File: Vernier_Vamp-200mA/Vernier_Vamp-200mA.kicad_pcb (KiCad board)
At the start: 4 copper layers, 143 x 99.5 mm, 203 parts, among them J1 Conn_01x02, J2 RJ45, J3 Screw_Terminal_01x04, J4 Conn_02x07_Odd_Even, J5 Conn_Coaxial, J6 Conn_Coaxial, J7 Conn_Coaxial, Q1 Si4447ADY, Q2 IRF8707PbF, SW1 DPDT_Hirose, U1 LM4040DBZ-5, U10 OPA2277, U11 OPA2277, U12 OPA2277, U13 OPA2277, U14 OPA2277, U15 OPA1622, U16 OPA1622, U17 OPA1622, U2 LM4040DBZ-5, U3 LM393, U4 TPS7A470x, U5 TPS7A470x, U6 TPS7A33, U7 LTC6655-2.5, U8 DAC8814, U9 OPA2277

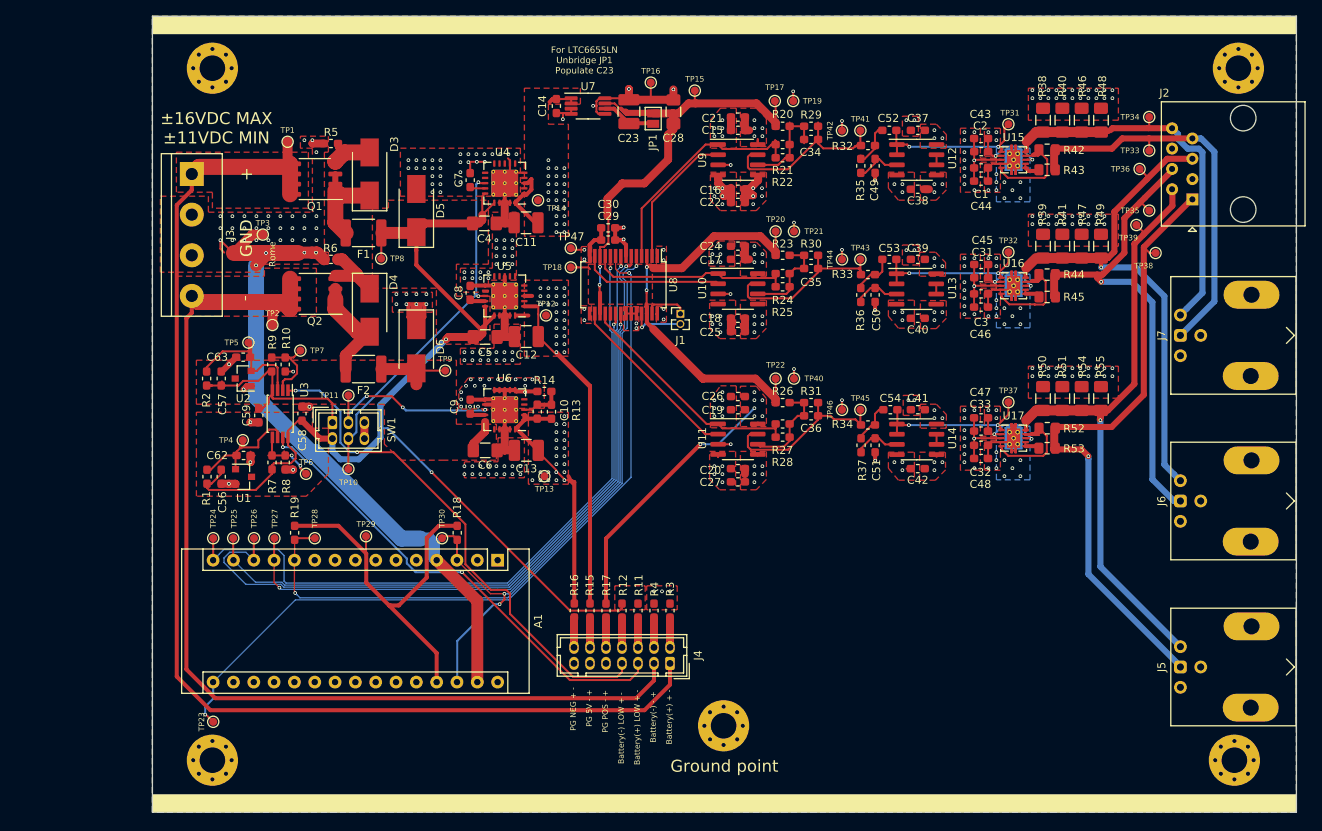
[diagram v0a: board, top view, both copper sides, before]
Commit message: Coil driver version 1.0B
Updated coil driver 200mA version with fixes requested by Iain.
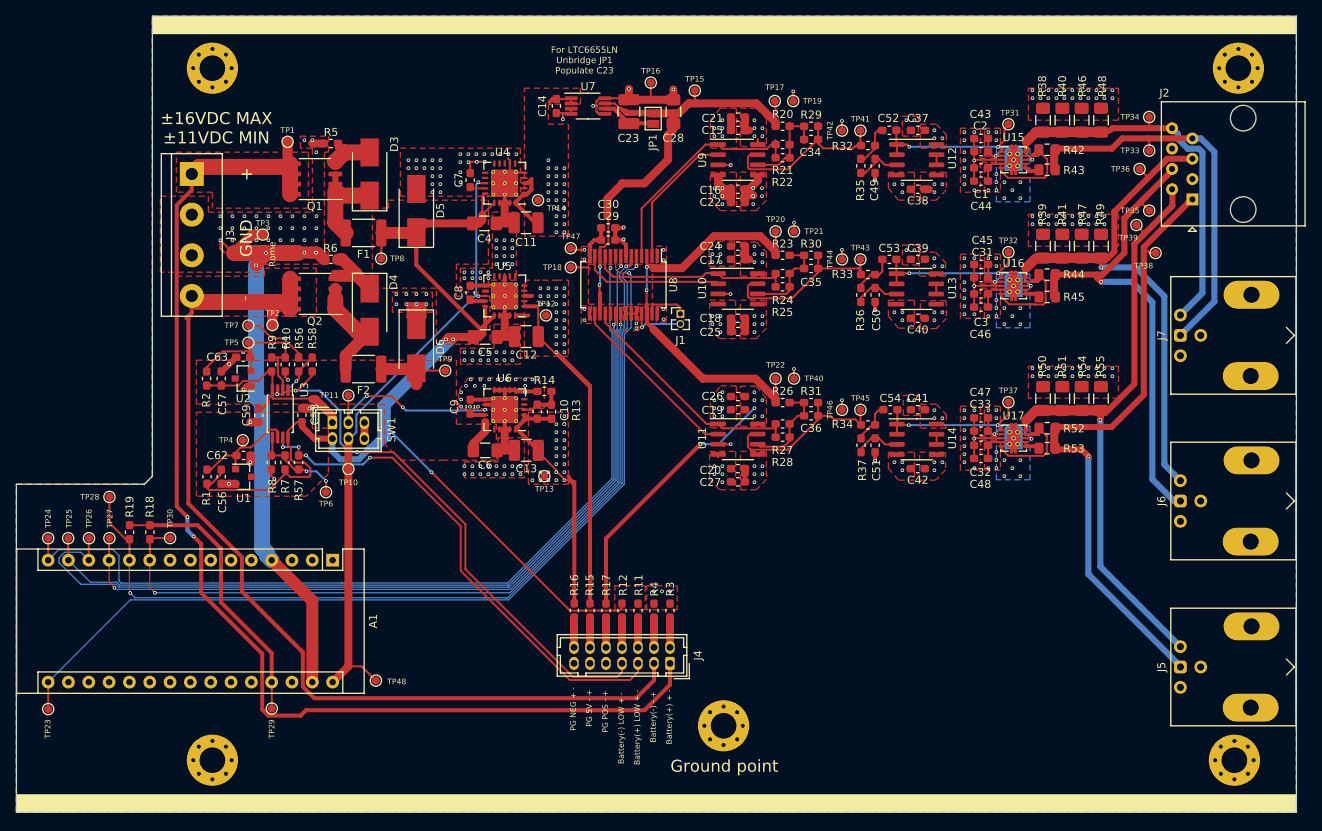
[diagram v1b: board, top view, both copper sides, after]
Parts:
- added R56: 3k, Resistor_SMD:R_0603_1608Metric_Pad1.05x0.95mm_HandSolder, F.Cu at (61.8, 91.3)
- added R57: 2M, Resistor_SMD:R_0603_1608Metric_Pad1.05x0.95mm_HandSolder, F.Cu at (61.8, 103.5)
- added R58: 133k, Resistor_SMD:R_0603_1608Metric_Pad1.05x0.95mm_HandSolder, F.Cu at (63.5, 91.3)
- added TP48: TestPoint_Probe, TestPoint:TestPoint_Pad_D1.0mm, F.Cu at (71.4, 130.8)
- R9: value 120k -> 133k
- moved R18 38.4 mm to (43.2, 112.2)
- moved TP30 34.0 mm to (45.7, 113.0)
- moved TP28 26.2 mm to (38.1, 107.8), turned to 0 degrees
- moved TP29 24.6 mm to (58.4, 134.3)
- moved TP23 20.7 mm to (30.5, 134.4)
- moved R19 20.6 mm to (40.6, 112.2)
- moved A1 20.6 mm to (66.0, 115.8)
- moved TP24 20.6 mm to (30.5, 113.0)
- moved TP25 20.6 mm to (33.0, 113.0)
- moved TP26 20.6 mm to (35.6, 113.0)
- moved TP27 20.6 mm to (38.1, 113.0)
- moved TP7 7.21 mm to (55.5, 86.4), turned to 180 degrees
- moved TP6 3.40 mm to (65.2, 107.2), turned to 180 degrees
- moved R8 1.74 mm to (58.4, 103.5)
- moved R7 1.62 mm to (60.1, 103.5)
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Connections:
- net +8V renamed +7V5
- net -8V renamed -7V5
- net /Power/+5V_c_ref renamed /Power/Battery_Management/+5V_c_ref
- net /Power/LED1_N renamed /Power/Battery_Management/Battery+_C
- net /Power/LED2_P renamed /Power/Battery_Management/Battery-_A
- net /Power/LED3_N renamed /Power/Battery_Management/Battery+_LOW_C
- net /Power/LED3_P renamed /Power/Battery_Management/Battery+_LOW_A
- net /Power/LED4_N renamed /Power/Battery_Management/Battery-_LOW_C
- net /Power/LED4_P renamed /Power/Battery_Management/Battery-_LOW_A
- net /Power/LED5_P renamed /Power/Battery_Management/+7.5_PG_A
- net /Power/LED6_P renamed /Power/Battery_Management/+5_PG_A
- net /Power/LED7_N renamed /Power/Battery_Management/-7.5_PG_C
- A1 pad 10: Net-(A1-Pad10) -> /DAC/~RS
- A1 pad 28: /DAC/~RS -> Net-(A1-Pad28)
- A1 pad 3: /DAC/~RS -> Net-(A1-Pad3)
- A1 pad 30: Net-(A1-Pad30) -> +12V_batt_post
- C63 pad 1: /Power/-5V_c_ref -> /Power/Battery_Management/-5V_c_ref
- R2 pad 1: /Power/-5V_c_ref -> /Power/Battery_Management/-5V_c_ref
- SW1 pad 4: /Power/+EN -> +12V_batt_post
- TP10 pad 1: /Power/+EN -> +12V_batt_post
- TP5 pad 1: /Power/-5V_c_ref -> /Power/Battery_Management/-5V_c_ref
- U2 pad 2: /Power/-5V_c_ref -> /Power/Battery_Management/-5V_c_ref
- U3 pad 3: /Power/-5V_c_ref -> Net-(R56-Pad1)
- U4 pad 13: /Power/+EN -> +12V_batt_post
- U5 pad 13: /Power/+EN -> +12V_batt_post
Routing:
- net +12V_batt_post: track 0.00 -> 76.6 mm, vias 0 -> 2
- net /Power/+EN: track 44.9 -> 0.00 mm, vias 2 -> 0
- net /DAC/~RS: track 76.1 -> 103.1 mm, vias 3 -> 2
- net /DAC/MSB: track 86.3 -> 111.2 mm
- net /Power/+12VDC_bat: track 143.0 -> 167.3 mm, vias 3 -> 4
- net /DAC/SDO: track 78.0 -> 98.6 mm
- net /DAC/SDI: track 90.2 -> 110.8 mm
- net /DAC/~LDAC: track 75.6 -> 96.3 mm
- net /DAC/~CS: track 91.9 -> 112.5 mm
- net /Power/Battery_Management/-5V_c_ref: track 0.00 -> 18.4 mm
- net /Power/-5V_c_ref: track 18.4 -> 0.00 mm
- net /DAC/CLK: track 97.8 -> 116.0 mm, vias 2 -> 1
- net +5VD: track 47.8 -> 35.4 mm
- net GNDD: track 67.8 -> 57.1 mm
- net -BATT: track 130.7 -> 123.6 mm
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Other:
- board size 143 x 99.5 mm -> 160 x 99.5 mm
- board text added: "Vernier Vamp 200mA Rev 1.0B Designer: Marcin Mrozowski EQOP"
- board text removed: "Vernier Vamp 200mA Rev 1.0A EQOP"

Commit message: Schematic and layout changes
Schematic updates:
- Added extra comments
- Added description (BNC channels)
- Moved mounting holes to the title block
- Added an option for connecting low battery indicatior LEDs to either +12V or GND (Comparator pulls to -12V)
- Added a 0R resistor for connecting +12V to Vin of nano
Layout:
- Added board ID and datecode on both sides
- Fixed priority of GND copper islands that were causing issues
- Changed the ground plane to be solid on the connection point (still not ideal but better)
- All components with thermal vias require tented vias so left as default
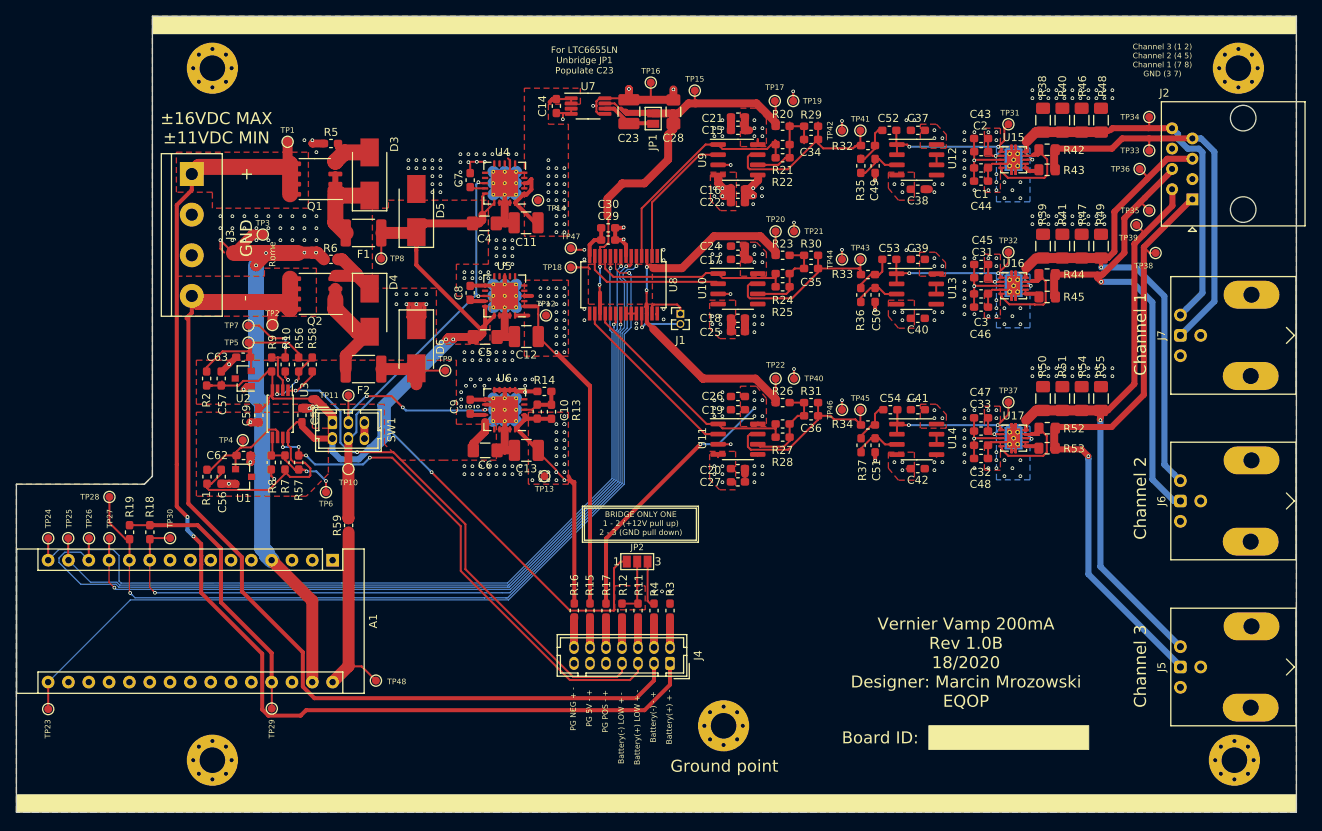
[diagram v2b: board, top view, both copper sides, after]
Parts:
- added JP2: SolderJumper_3_Open, Jumper:SolderJumper-3_P1.3mm_Open_Pad1.0x1.5mm_NumberLabels, F.Cu at (104.1, 115.9)
- added R59: 0R, Resistor_SMD:R_0603_1608Metric_Pad1.05x0.95mm_HandSolder, F.Cu at (68.0, 111.4)
- J5: value Conn_Coaxial -> Channel 3
- J6: value Conn_Coaxial -> Channel 2
- J7: value Conn_Coaxial -> Channel 1
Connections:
- A1 pad 30: +12V_batt_post -> Net-(A1-Pad30)
- R11 pad 1: /Power/+12VDC_bat -> Net-(JP2-Pad2)
- R12 pad 1: /Power/+12VDC_bat -> Net-(JP2-Pad2)
- TP48 pad 1: +12V_batt_post -> Net-(A1-Pad30)
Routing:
- net GND: track 178.5 -> 225.6 mm, vias 316 -> 321
- net Net-(A1-Pad30): track 0.00 -> 26.5 mm
- net +12V_batt_post: track 76.6 -> 51.1 mm
- net Net-(JP2-Pad2): track 0.00 -> 7.29 mm
- net /Power/+12VDC_bat: track 167.3 -> 172.8 mm
- net +7V5: vias 65 -> 60
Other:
- board text added: "BRIDGE ONLY ONE 1 - 2 (+12V pull up) 2 - 3 (GND pull down)"
- board text added: "Board ID:"
- board text added: "Channel 1"
- board text added: "Channel 2"
- board text added: "Channel 3"
- board text added: "Channel 3 (1 2) Channel 2 (4 5) Channel 1 (7 8) GND (3 7)"
- board text added: "Vernier Vamp 200mA Rev 1.0B 18/2020 Designer: Marcin Mrozowski EQOP"
- board text removed: "Vernier Vamp 200mA Rev 1.0B Designer: Marcin Mrozowski EQOP"

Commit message: Silkscreen change
Changed the date code to month/year format.
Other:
- board text added: "Vernier Vamp 200mA Rev 1.0B April 2020"
- board text added: "Vernier Vamp 200mA Rev 1.0B April 2020 Designer: Marcin Mrozowski EQOP"
- board text removed: "Vernier Vamp 200mA Rev 1.0B 18/2020 Designer: Marcin Mrozowski EQOP"
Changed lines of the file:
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@@
   )
   (setup
-    (last_trace_width 0.254)
+    (last_trace_width 0.127)
     (user_trace_width 0.127)
     (user_trace_width 0.254)
@@
     (effects (font (size 0.7 0.7) (thickness 0.1)))
   )
-  (gr_text "Vernier Vamp 200mA\nRev 1.0B\n18/2020\nDesigner: Marcin Mrozowski\nEQOP" (at 145.2 128.55) (layer F.SilkS)
+  (gr_text "Vernier Vamp 200mA\nRev 1.0B\nApril 2020" (at 145.2 128.55) (layer F.SilkS)
     (effects (font (size 1.5 1.5) (thickness 0.3)))
   )
@@
     (effects (font (size 0.7 0.7) (thickness 0.127)))
   )
-  (gr_text "Vernier Vamp 200mA\nRev 1.0B\n18/2020\nDesigner: Marcin Mrozowski\nEQOP" (at 145.25 128.6) (layer B.SilkS)
+  (gr_text "Vernier Vamp 200mA\nRev 1.0B\nApril 2020\nDesigner: Marcin Mrozowski\nEQOP" (at 145.25 128.6) (layer B.SilkS)
     (effects (font (size 1.5 1.5) (thickness 0.3)) (justify mirror))
   )
@@
   (segment (start 87.541 96.94) (end 86.116 98.365) (width 1.5) (layer B.Cu) (net 26))
   (segment (start 87.541 96.94) (end 86.196601 96.94) (width 1.5) (layer B.Cu) (net 26))
+  (via (at 95 68.75) (size 0.4572) (drill 0.254) (layers F.Cu B.Cu) (net 26))
+  (via (at 95 67.75) (size 0.4572) (drill 0.254) (layers F.Cu B.Cu) (net 26))
+  (via (at 95 66.75) (size 0.4572) (drill 0.254) (layers F.Cu B.Cu) (net 26))
+  (via (at 94 66.75) (size 0.4572) (drill 0.254) (layers F.Cu B.Cu) (net 26))
+  (via (at 94 67.75) (size 0.4572) (drill 0.254) (layers F.Cu B.Cu) (net 26))
+  (segment (start 105.725 121.175) (end 106.2 121.175) (width 0.254) (layer F.Cu) (net 26))
+  (segment (start 105.4 120.85) (end 105.725 121.175) (width 0.254) (layer F.Cu) (net 26))
+  (segment (start 105.4 115.925) (end 105.4 120.85) (width 0.254) (layer F.Cu) (net 26))
   (segment (start 83.379 69.269) (end 83.223 69.113) (width 0.254) (layer F.Cu) (net 27))
   (segment (start 85.091 69.269) (end 83.379 69.269) (width 0.254) (layer F.Cu) (net 27))
@@
   (segment (start 72.8 100.35) (end 71.4 101.75) (width 1) (layer B.Cu) (net 89))
   (segment (start 71.4 101.75) (end 70.760254 101.75) (width 1) (layer B.Cu) (net 89))
+  (segment (start 101.2 116.771) (end 101.2 122.05) (width 0.254) (layer F.Cu) (net 89))
+  (segment (start 102.046 115.925) (end 101.2 116.771) (width 0.254) (layer F.Cu) (net 89))
+  (segment (start 102.8 115.925) (end 102.046 115.925) (width 0.254) (layer F.Cu) (net 89))
+  (segment (start 95.7 122.05) (end 101.2 122.05) (width 0.254) (layer F.Cu) (net 89))
   (segment (start 85.091 82.716) (end 84.284 82.716) (width 0.254) (layer F.Cu) (net 92))
   (via (at 84.25 82.75) (size 0.4572) (drill 0.254) (layers F.Cu B.Cu) (net 92))
@@
   (segment (start 68 110.5) (end 68.025 110.525) (width 1.5) (layer F.Cu) (net 92))
   (segment (start 68 104.35) (end 68 110.5) (width 1.5) (layer F.Cu) (net 92))
-  (segment (start 69.6535 129.017) (end 71.44 130.8035) (width 0.254) (layer F.Cu) (net 110))
-  (segment (start 68 129.017) (end 69.6535 129.017) (width 0.254) (layer F.Cu) (net 110))
-  (segment (start 68 129.017) (end 66.027 130.99) (width 1) (layer F.Cu) (net 110))
   (segment (start 60.975 130.962) (end 60.947 130.99) (width 0.254) (layer B.Cu) (net 93))
   (via (at 114.75 69.25) (size 0.4572) (drill 0.254) (layers F.Cu B.Cu) (net 95))
@@
   (via (at 94 70.75) (size 0.4572) (drill 0.254) (layers F.Cu B.Cu) (net 96))
   (via (at 95 69.75) (size 0.4572) (drill 0.254) (layers F.Cu B.Cu) (net 96))
-  (via (at 95 68.75) (size 0.4572) (drill 0.254) (layers F.Cu B.Cu) (net 26))
   (via (at 94 68.75) (size 0.4572) (drill 0.254) (layers F.Cu B.Cu) (net 96))
-  (via (at 95 67.75) (size 0.4572) (drill 0.254) (layers F.Cu B.Cu) (net 26))
-  (via (at 95 66.75) (size 0.4572) (drill 0.254) (layers F.Cu B.Cu) (net 26))
-  (via (at 94 66.75) (size 0.4572) (drill 0.254) (layers F.Cu B.Cu) (net 26))
   (via (at 93 66.75) (size 0.4572) (drill 0.254) (layers F.Cu B.Cu) (net 96))
   (via (at 93 67.75) (size 0.4572) (drill 0.254) (layers F.Cu B.Cu) (net 96))
@@
   (segment (start 117.567 78.144) (end 118.092 78.144) (width 1) (layer F.Cu) (net 96))
   (via (at 94 69.75) (size 0.4572) (drill 0.254) (layers F.Cu B.Cu) (net 96))
-  (via (at 94 67.75) (size 0.4572) (drill 0.254) (layers F.Cu B.Cu) (net 26))
-  (segment (start 105.725 121.175) (end 106.2 121.175) (width 0.254) (layer F.Cu) (net 26))
-  (segment (start 105.4 120.85) (end 105.725 121.175) (width 0.254) (layer F.Cu) (net 26))
-  (segment (start 105.4 115.925) (end 105.4 120.85) (width 0.254) (layer F.Cu) (net 26))
-  (segment (start 101.2 116.771) (end 101.2 122.05) (width 0.254) (layer F.Cu) (net 89))
-  (segment (start 102.046 115.925) (end 101.2 116.771) (width 0.254) (layer F.Cu) (net 89))
-  (segment (start 102.8 115.925) (end 102.046 115.925) (width 0.254) (layer F.Cu) (net 89))
-  (segment (start 95.7 122.05) (end 101.2 122.05) (width 0.254) (layer F.Cu) (net 89))
   (via (at 118.75 60.75) (size 0.4572) (drill 0.254) (layers F.Cu B.Cu) (net 96))
   (via (at 118.75 61.75) (size 0.4572) (drill 0.254) (layers F.Cu B.Cu) (net 96))
@@
   (segment (start 61.788 93.07688) (end 61.49844 93.36644) (width 0.254) (layer F.Cu) (net 109))
   (segment (start 61.788 92.1619) (end 61.788 93.07688) (width 0.254) (layer F.Cu) (net 109))
+  (segment (start 69.6535 129.017) (end 71.44 130.8035) (width 0.254) (layer F.Cu) (net 110))
+  (segment (start 68 129.017) (end 69.6535 129.017) (width 0.254) (layer F.Cu) (net 110))
+  (segment (start 68 129.017) (end 66.027 130.99) (width 1) (layer F.Cu) (net 110))
   (segment (start 68.025 128.992) (end 66.027 130.99) (width 1.5) (layer F.Cu) (net 110))
   (segment (start 68.025 112.275) (end 68.025 128.992) (width 1.5) (layer F.Cu) (net 110))
